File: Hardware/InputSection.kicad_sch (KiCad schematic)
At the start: 14 parts, among them SW1 SW_Push, SW2 SW_Push, SW3 SW_Push, SW4 SW_Push

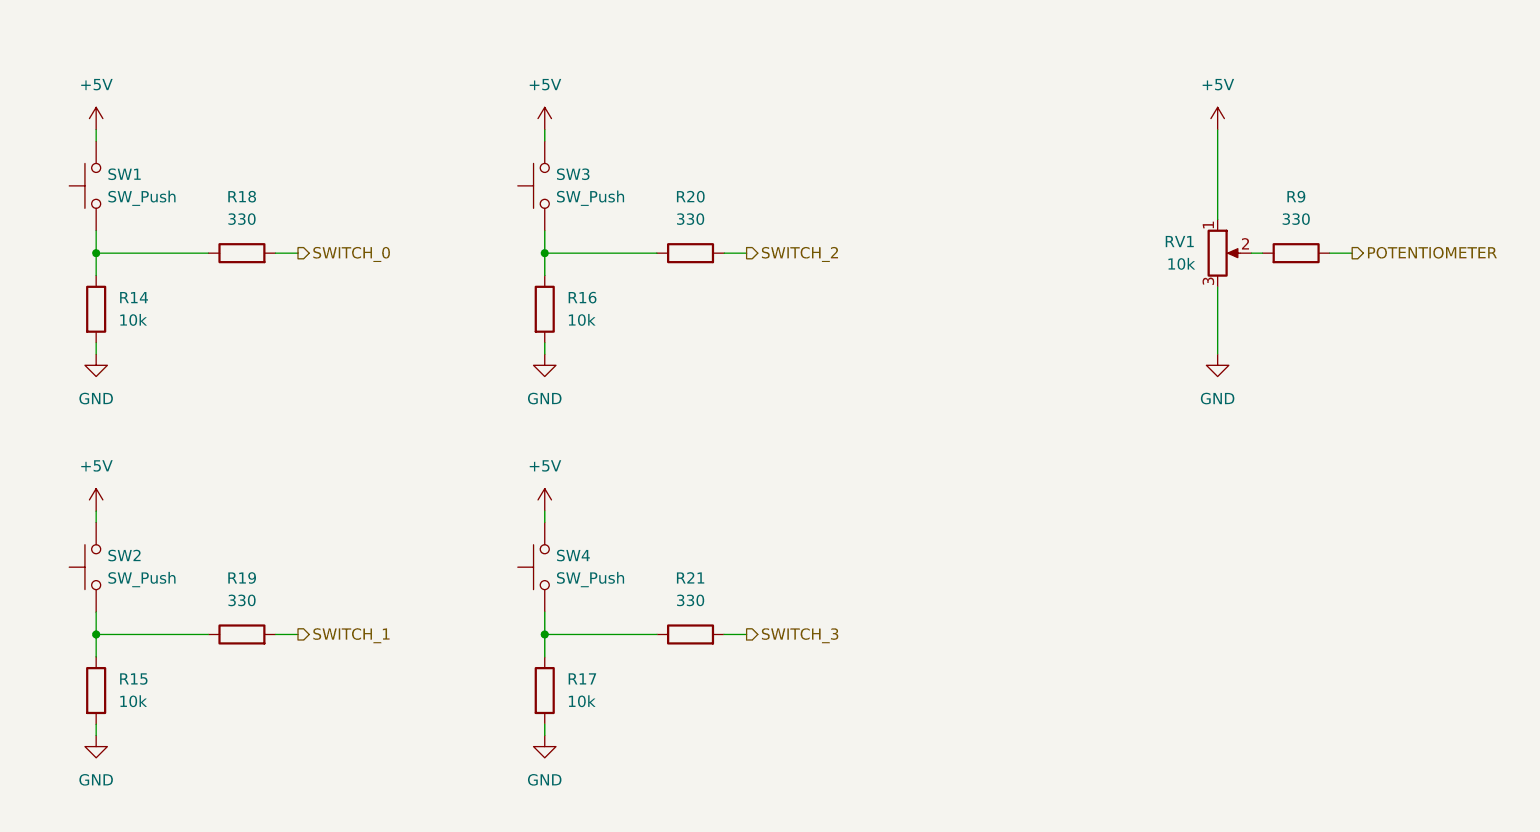
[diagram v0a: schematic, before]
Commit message: Updated KiCAD project.
- Added grouping in schematics.
- Removed unnecessary net names in "LogicSection.kicad_sch".
- Added 330R between +5V and nREG_ENABLE.
- Changed path for 3D models.
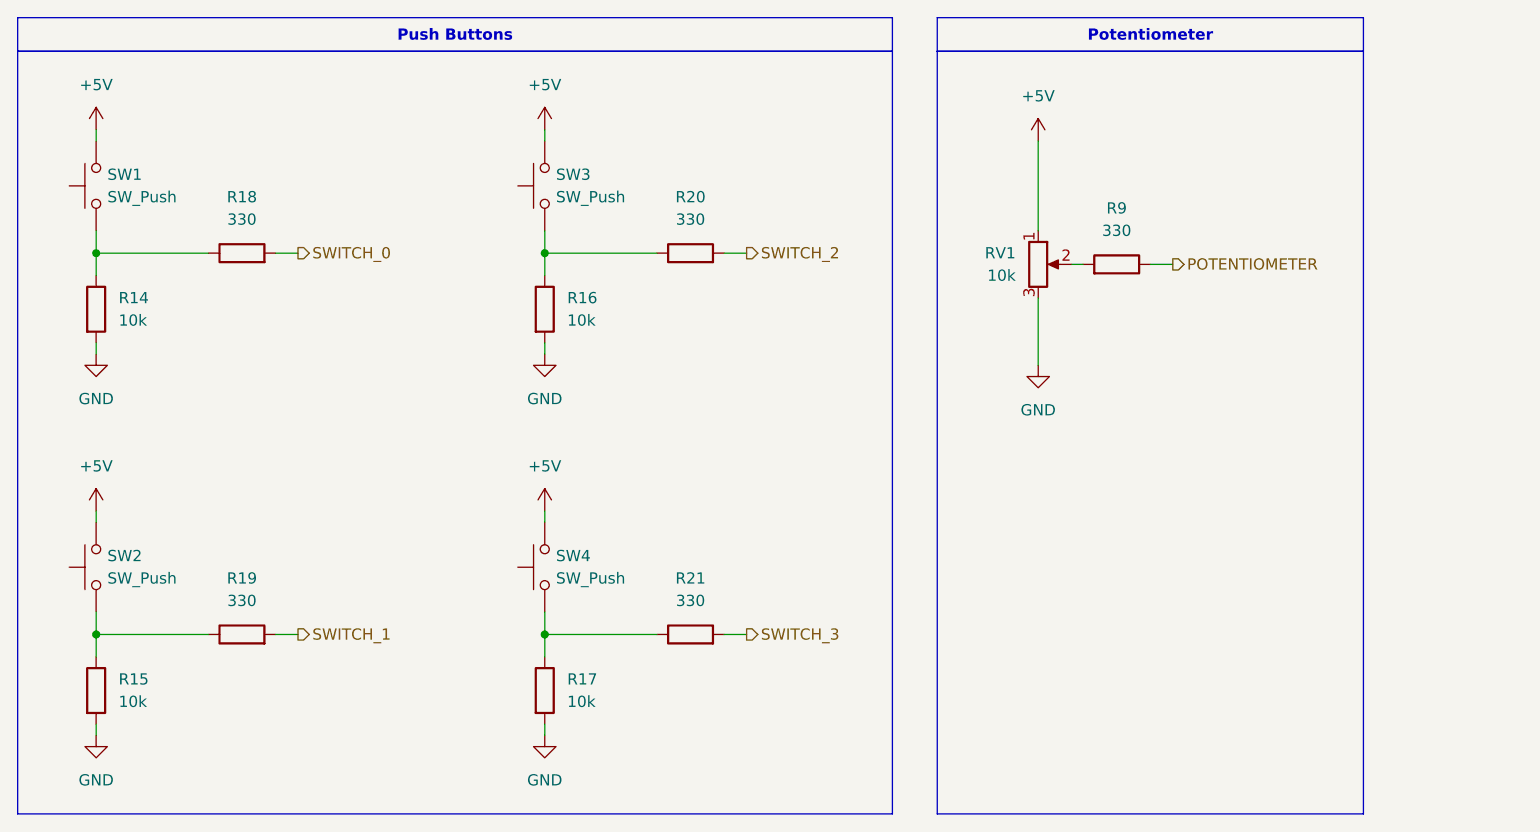
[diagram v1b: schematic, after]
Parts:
- RV1: MPN (none) -> RM065-103
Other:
- moved on the sheet: R9, RV1
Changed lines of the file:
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@@
 	(title_block
 		(title "Simon")
-		(date "2026-03-20")
+		(date "2026-03-31")
 		(rev "01")
 		(company "Kaffeklubben Labs")
+	)
+	(rectangle
+		(start 171.45 60.96)
+		(end 219.71 147.32)
+		(stroke
+			(width 0)
+			(type default)
+		)
+		(fill
+			(type none)
+		)
+	)
+	(rectangle
+		(start 67.31 60.96)
+		(end 166.37 147.32)
+		(stroke
+			(width 0)
+			(type default)
+		)
+		(fill
+			(type none)
+		)
+	)
+	(text_box "Push Buttons"
+		(exclude_from_sim no)
+		(at 67.31 57.15 0)
+		(size 99.06 3.81)
+		(margins 0.9525 0.9525 0.9525 0.9525)
+		(stroke
+			(width 0)
+			(type solid)
+		)
+		(fill
+			(type color)
+			(color 0 0 194 1)
+		)
+		(effects
+			(font
+				(face "Consolas")
+				(size 1.27 1.27)
+				(bold yes)
+				(color 255 255 255 1)
+			)
+		)
+	)
+	(text_box "Potentiometer"
+		(exclude_from_sim no)
+		(at 171.45 57.15 0)
+		(size 48.26 3.81)
+		(margins 0.9525 0.9525 0.9525 0.9525)
+		(stroke
+			(width 0)
+			(type solid)
+		)
+		(fill
+			(type color)
+			(color 0 0 194 1)
+		)
+		(effects
+			(font
+				(face "Consolas")
+				(size 1.27 1.27)
+				(bold yes)
+				(color 255 255 255 1)
+			)
+		)
 	)
 	(junction
@@
 	(wire
 		(pts
-			(xy 218.44 83.82) (xy 215.9 83.82)
+			(xy 198.12 85.09) (xy 195.58 85.09)
 		)
 		(stroke
@@
 	(wire
 		(pts
-			(xy 203.2 69.85) (xy 203.2 80.01)
+			(xy 182.88 71.12) (xy 182.88 81.28)
 		)
 		(stroke
@@
 	(wire
 		(pts
-			(xy 203.2 87.63) (xy 203.2 95.25)
+			(xy 182.88 88.9) (xy 182.88 96.52)
 		)
 		(stroke
@@
 	(wire
 		(pts
-			(xy 208.28 83.82) (xy 207.01 83.82)
+			(xy 187.96 85.09) (xy 186.69 85.09)
 		)
 		(stroke
@@
 	(hierarchical_label "POTENTIOMETER"
 		(shape output)
-		(at 218.44 83.82 0)
+		(at 198.12 85.09 0)
 		(effects
 			(font
@@
 	(symbol
 		(lib_id "power:+5V")
-		(at 203.2 69.85 0)
+		(at 182.88 71.12 0)
 		(mirror y)
 		(unit 1)
@@
 		(fields_autoplaced yes)
 		(property "Reference" "#PWR012"
-			(at 203.2 73.66 0)
+			(at 182.88 74.93 0)
 			(hide yes)
 			(show_name no)
@@
 		)
 		(property "Value" "+5V"
-			(at 203.2 64.77 0)
+			(at 182.88 66.04 0)
 			(show_name no)
 			(do_not_autoplace no)
@@
 		)
 		(property "Footprint" ""
-			(at 203.2 69.85 0)
+			(at 182.88 71.12 0)
 			(hide yes)
 			(show_name no)
@@
 		)
 		(property "Datasheet" ""
-			(at 203.2 69.85 0)
+			(at 182.88 71.12 0)
 			(hide yes)
 			(show_name no)
@@
 		)
 		(property "Description" "Power symbol creates a global label with name \"+5V\""
-			(at 203.2 69.85 0)
+			(at 182.88 71.12 0)
 			(hide yes)
 			(show_name no)
@@
 	(symbol
 		(lib_id "Device:R_Potentiometer")
-		(at 203.2 83.82 0)
+		(at 182.88 85.09 0)
 		(unit 1)
 		(body_style 1)
@@
 		(fields_autoplaced yes)
 		(property "Reference" "RV1"
-			(at 200.66 82.5499 0)
+			(at 180.34 83.8199 0)
 			(show_name no)
 			(do_not_autoplace no)
@@
 		)
 		(property "Value" "10k"
-			(at 200.66 85.0899 0)
+			(at 180.34 86.3599 0)
 			(show_name no)
 			(do_not_autoplace no)
@@
 		)
 		(property "Footprint" "Potentiometer_THT:Potentiometer_Runtron_RM-065_Vertical"
-			(at 203.2 83.82 0)
+			(at 182.88 85.09 0)
 			(hide yes)
 			(show_name no)
@@
 		)
 		(property "Datasheet" ""
-			(at 203.2 83.82 0)
+			(at 182.88 85.09 0)
 			(hide yes)
 			(show_name no)
@@
 		)
 		(property "Description" "Potentiometer"
-			(at 203.2 83.82 0)
+			(at 182.88 85.09 0)
 			(hide yes)
 			(show_name no)
@@
 		)
 		(property "LCSC" ""
-			(at 203.2 83.82 0)
-			(hide yes)
-			(show_name no)
-			(do_not_autoplace no)
-			(effects
-				(font
-					(size 1.27 1.27)
-				)
-			)
-		)
-		(property "MPN" ""
-			(at 203.2 83.82 0)
+			(at 182.88 85.09 0)
+			(hide yes)
+			(show_name no)
+			(do_not_autoplace no)
+			(effects
+				(font
+					(size 1.27 1.27)
+				)
+			)
+		)
+		(property "MPN" "RM065-103"
+			(at 182.88 85.09 0)
+			(hide yes)
+			(show_name no)
+			(do_not_autoplace no)
+			(effects
+				(font
+					(size 1.27 1.27)
+				)
+			)
+		)
+		(property "Sim.Device" "R"
+			(at 182.88 85.09 0)
+			(hide yes)
+			(show_name no)
+			(do_not_autoplace no)
+			(effects
+				(font
+					(size 1.27 1.27)
+				)
+			)
+		)
+		(property "Sim.Type" "POT"
+			(at 182.88 85.09 0)
+			(hide yes)
+			(show_name no)
+			(do_not_autoplace no)
+			(effects
+				(font
+					(size 1.27 1.27)
+				)
+			)
+		)
+		(property "Sim.Pins" "1=r0 2=wiper 3=r1"
+			(at 182.88 85.09 0)
 			(hide yes)
 			(show_name no)
@@
 	(symbol
 		(lib_id "Device:R")
-		(at 212.09 83.82 270)
+		(at 191.77 85.09 270)
 		(mirror x)
 		(unit 1)
@@
 		(fields_autoplaced yes)
 		(property "Reference" "R9"
-			(at 212.09 77.47 90)
+			(at 191.77 78.74 90)
 			(show_name no)
 			(do_not_autoplace no)
@@
 		)
 		(property "Value" "330"
-			(at 212.09 80.01 90)
+			(at 191.77 81.28 90)
 			(show_name no)
 			(do_not_autoplace no)
@@
 		)
 		(property "Footprint" "Resistor_SMD:R_0805_2012Metric"
-			(at 212.09 85.598 90)
+			(at 191.77 86.868 90)
 			(hide yes)
 			(show_name no)
@@
 		)
 		(property "Datasheet" ""
-			(at 212.09 83.82 0)
+			(at 191.77 85.09 0)
 			(hide yes)
 			(show_name no)
@@
 		)
 		(property "Description" "Resistor"
-			(at 212.09 83.82 0)
+			(at 191.77 85.09 0)
 			(hide yes)
 			(show_name no)
@@
 		)
 		(property "LCSC" ""
-			(at 212.09 83.82 90)
+			(at 191.77 85.09 90)
 			(hide yes)
 			(show_name no)
@@
 		)
 		(property "MPN" ""
-			(at 212.09 83.82 90)
+			(at 191.77 85.09 90)
 			(hide yes)
 			(show_name no)
@@
 	(symbol
 		(lib_id "power:GND")
-		(at 203.2 95.25 0)
+		(at 182.88 96.52 0)
 		(mirror y)
 		(unit 1)
@@
 		(fields_autoplaced yes)
 		(property "Reference" "#PWR011"
-			(at 203.2 101.6 0)
+			(at 182.88 102.87 0)
 			(hide yes)
 			(show_name no)
@@
 		)
 		(property "Value" "GND"
-			(at 203.2 100.33 0)
+			(at 182.88 101.6 0)
 			(show_name no)
 			(do_not_autoplace no)
@@
 		)
 		(property "Footprint" ""
-			(at 203.2 95.25 0)
+			(at 182.88 96.52 0)
 			(hide yes)
 			(show_name no)
@@
 		)
 		(property "Datasheet" ""
-			(at 203.2 95.25 0)
+			(at 182.88 96.52 0)
 			(hide yes)
 			(show_name no)
@@
 		)
 		(property "Description" "Power symbol creates a global label with name \"GND\" , ground"
-			(at 203.2 95.25 0)
-			(hide yes)
-			(show_name no)
+			(at 182.88 96.52 0)
+			(hide yes)
+			(show_name no)
